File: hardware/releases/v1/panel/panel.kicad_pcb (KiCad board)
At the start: 4 copper layers, 124.5 x 55.6 mm, 171 parts, among them J1 12-32V + RS485, J101 Main board, J102 XD_North, J103 XD_East, J104 XD_South, J105 XD_West, J106 PIEZO_NE, J107 PIEZO_NW, J108 PIEZO_SW, J109 PIEZO_SE, J110 DOME_SOCKET, J111 AUX 5V_HEAT, J2 Crown board, J201 Probe T-Header SMD, J3 Probe board, J301 CROWN_RISER, J4 PMSA003I PM, J401 Main board, J402 Reflector T-Socket SMD, J5 Power board, J501 Main board, Q1 AO3400A, Q401 AO3400A, SW1 SERVICE, U101 SN74LVC2G04DBVR, U102 CD4052BM96, U103 TLV9062IDR, U104 LM393DR2G, U105 TLV9062IDR, U106 MMC5603NJ, U2 LM66100, U3 XIAO ESP32C6, U301 LTR-390UV-01, U302 TSL25911FN, U303 GUVB-C31SM, U4 ADS1115IDGSR, U401 SCD41-D-R2, U402 SGP41-D-R4, U403 SHT40-AD1F-R2, U404 LM393DR2G, U405 BMP585, U5 LSM6DS3TR-C, U501 SCT2430STER, U502 SCT2430STER, U6 AS3935-BQFT, U7 SP3485EN-L/TR, U8 SN74LVC2G04DBVR

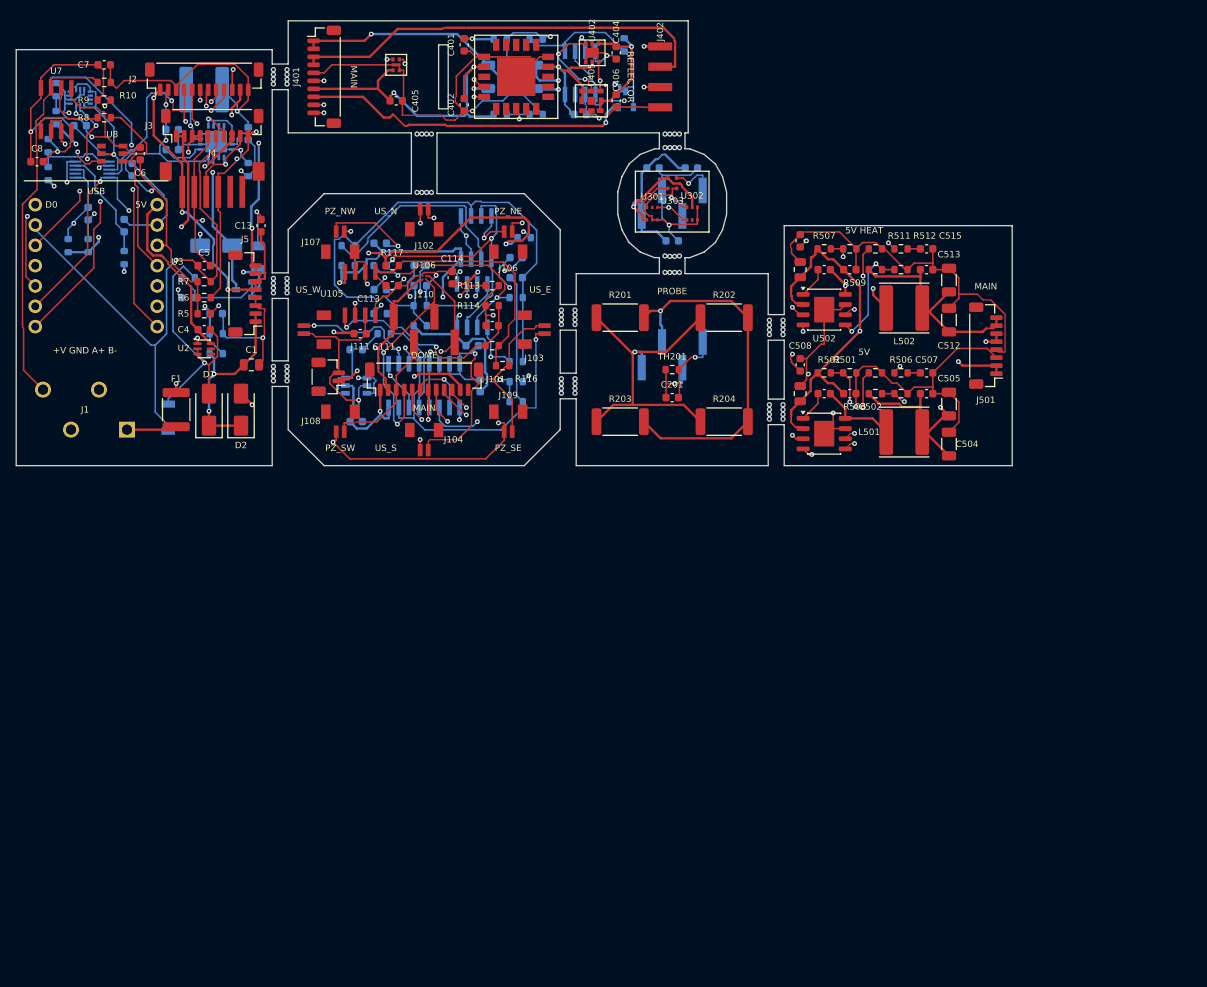
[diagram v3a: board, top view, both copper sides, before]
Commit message: Update documentation for 60V power system, STM32 crown board, 12V heaters, and expanded enclosure design
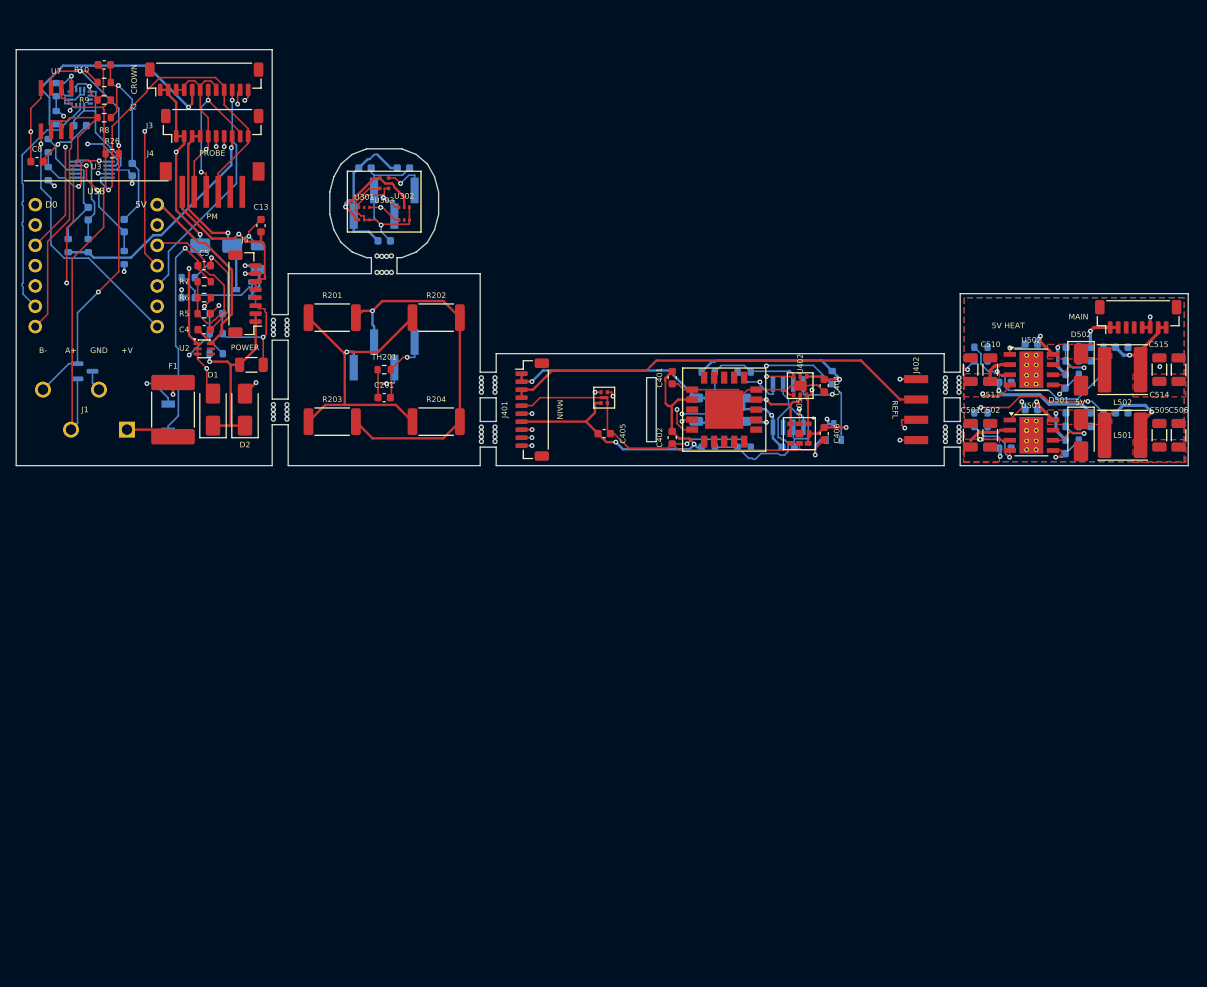
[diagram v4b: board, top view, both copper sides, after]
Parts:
- removed C10: 1u 50V, Capacitor_SMD:C_0603_1608Metric
- removed C101, C102, C103, C104, C105, C11, C110, C111, C114, C6: 100n 50V, Capacitor_SMD:C_0603_1608Metric
- removed C106, C107, C109: 47n 50V, Capacitor_SMD:C_0603_1608Metric
- removed C108, C112: 18p C0G 50V, Capacitor_SMD:C_0603_1608Metric
- removed C113: 220n 50V, Capacitor_SMD:C_0603_1608Metric
- removed C12: 470p C0G 50V, Capacitor_SMD:C_0603_1608Metric
- removed J101: Main board, Connector_JST:JST_SH_BM12B-SRSS-TB_1x12-1MP_P1.00mm_Vertical
- removed J102: XD_North, gateway_fp:JST_BM02B-SRSS-TB
- removed J103: XD_East, gateway_fp:JST_BM02B-SRSS-TB
- removed J104: XD_South, gateway_fp:JST_BM02B-SRSS-TB
- removed J105: XD_West, gateway_fp:JST_BM02B-SRSS-TB
- removed J106: PIEZO_NE, gateway_fp:JST_BM02B-SRSS-TB
- removed J107: PIEZO_NW, gateway_fp:JST_BM02B-SRSS-TB
- removed J108: PIEZO_SW, gateway_fp:JST_BM02B-SRSS-TB
- removed J109: PIEZO_SE, gateway_fp:JST_BM02B-SRSS-TB
- removed J110: DOME_SOCKET, gateway_fp:HX_PZ2.54-1x4P-SMD
- removed J111: AUX 5V_HEAT, Connector_JST:JST_SH_BM02B-SRSS-TB_1x02-1MP_P1.00mm_Vertical
- removed L2: 220uH, Inductor_SMD:L_Sunlord_SWPA6045S
- removed R101, R104, R105, R108, R113: 1k, Resistor_SMD:R_0603_1608Metric
- removed R102, R103, R107, R11, R111, R115: 10k, Resistor_SMD:R_0603_1608Metric
- removed R106, R109: 22k, Resistor_SMD:R_0603_1608Metric
- removed R110, R114, R117: 100k, Resistor_SMD:R_0603_1608Metric
- removed R112: 4k7, Resistor_SMD:R_0603_1608Metric
- removed R116: 20k, Resistor_SMD:R_0603_1608Metric
- removed U101, U8: SN74LVC2G04DBVR, gateway_fp:TI_SN74LVC2G04_SOT-23-6
- removed U102: CD4052BM96, gateway_fp:TI_CD4052BM96_SOIC-16
- removed U103, U105: TLV9062IDR, gateway_fp:TI_TLV9062IDR_SOIC-8
- removed U104: LM393DR2G, gateway_fp:ON_LM393DR2G_SOIC-8
- removed U106: MMC5603NJ, gateway_fp:MEMSIC_MMC5603NJ_WLCSP-4
- removed U6: AS3935-BQFT, gateway_fp:ScioSense_AS3935_QFN-16
- added C517: 18n 50V, Capacitor_SMD:C_0603_1608Metric, B.Cu at (135.1, -13.1)
- added C518: 68p C0G 50V, Capacitor_SMD:C_0603_1608Metric, B.Cu at (132.0, -14.8)
- added D4: PSM712, Package_TO_SOT_SMD:SOT-23, B.Cu at (8.60, -11.8)
- added D501: B360A, Diode_SMD:D_SMA, F.Cu at (133.1, -3.80)
- added D502: B360A, Diode_SMD:D_SMA, F.Cu at (133.1, -12.0)
- added R26: 120R, Resistor_SMD:R_0603_1608Metric, F.Cu at (12.0, -39.0)
- C1, C501: value 10u 50V -> 2u2 100V; footprint Capacitor_SMD:C_0805_2012Metric -> Capacitor_SMD:C_1206_3216Metric
- C502, C510, C511: value 100n 50V -> 2u2 100V; footprint Capacitor_SMD:C_0603_1608Metric -> Capacitor_SMD:C_1206_3216Metric
- C503: value 100n 50V -> 100n 100V; moved to B.Cu
- C504, C513: value 47u 10V -> 100n 50V; footprint Capacitor_SMD:C_1206_3216Metric -> Capacitor_SMD:C_0603_1608Metric; moved to B.Cu
- C506: value 100n 50V -> 47u 10V; footprint Capacitor_SMD:C_0603_1608Metric -> Capacitor_SMD:C_1206_3216Metric
- C507: value 3n3 50V -> 100n 50V; moved to B.Cu
- C508: value 22p C0G 50V -> 33n 50V; moved to B.Cu
- C509: value 10u 50V -> 68p C0G 50V; footprint Capacitor_SMD:C_0805_2012Metric -> Capacitor_SMD:C_0603_1608Metric; moved to B.Cu
- C512: value 47u 10V -> 100n 100V; footprint Capacitor_SMD:C_1206_3216Metric -> Capacitor_SMD:C_0603_1608Metric; moved to B.Cu
- C514: value 100n 50V -> 22u 25V; footprint Capacitor_SMD:C_0603_1608Metric -> Capacitor_SMD:C_1206_3216Metric
- C515: value 3n3 50V -> 22u 25V; footprint Capacitor_SMD:C_0603_1608Metric -> Capacitor_SMD:C_1206_3216Metric
- C516: value 22p C0G 50V -> 100n 50V; moved to B.Cu
- D1: value SMAJ33A -> SMAJ36A
- F1: footprint Fuse:Fuse_1812_4532Metric -> Fuse:Fuse_2920_7451Metric
- L502: value 8.2uH -> 22uH
- R10, R9: value 4k7 -> 390R
- R20: value 10k -> 30k
- R201, R202, R203, R204: value 27R -> 120R
- R401, R402: value 120R -> 680R
- R5, R6: value 4k7 -> 2k2
- R501, R507: value 51k -> 511k; moved to B.Cu
- R502, R508: value 10k -> 82k5; moved to B.Cu
- R503, R504: moved to B.Cu
- R505, R511: value 200k -> 130k; moved to B.Cu
- R506, R512: value 33k2 -> 6k49; moved to B.Cu
- R509: value 53k6 -> 140k; moved to B.Cu
- R510: value 10k2 -> 10k; moved to B.Cu
- R8: value 1k -> 10k
- U404: value LM393DR2G -> LM2903DR2G
- U501, U502: value SCT2430STER -> TPS54360DDAR; footprint Package_SO:SOIC-8-1EP_3.9x4.9mm_P1.27mm_EP2.514x3.2mm -> Package_SO:TI_SO-PowerPAD-8_ThermalVias
- moved J402 52.5 mm to (112.5, -7.00)
- moved C401 49.1 mm to (82.0, -11.0)
- moved C402 49.1 mm to (82.0, -3.50)
- moved C403 49.1 mm to (96.5, -2.30)
- moved C404 49.1 mm to (101.0, -10.0)
- moved C405 49.1 mm to (73.5, -4.00)
- moved C406 49.1 mm to (101.0, -4.00)
- moved J401 49.1 mm to (64.5, -7.00)
- moved Q401 49.1 mm to (102.2, -4.20)
- moved R401 49.1 mm to (85.0, -7.00)
- moved R402 49.1 mm to (91.0, -7.00)
- moved R403 49.1 mm to (86.5, -11.7)
- moved R404 49.1 mm to (86.5, -2.30)
- moved R405 49.1 mm to (91.0, -2.30)
- moved R406 49.1 mm to (102.0, -11.0)
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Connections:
- net REFLECTOR_+5V_HEAT renamed REFLECTOR_+12V_HEAT
- C403 pad 1: PROBE_+3V3 -> PROBE_+12V_HEAT
- C503 pad 1: POWER_LOGIC_BST -> POWER_VIN_PROT
- C503 pad 2: POWER_LOGIC_SW -> POWER_GND
- C504 pad 1: POWER_+5V -> POWER_LOGIC_BST
- C504 pad 2: POWER_GND -> POWER_LOGIC_SW
- C507 pad 1: POWER_LOGIC_CC -> POWER_+5V
- C508 pad 1: POWER_LOGIC_COMP -> POWER_LOGIC_CC
- C509 pad 1: POWER_VIN_PROT -> POWER_LOGIC_COMP
- C511 pad 1: POWER_HEAT_BST -> POWER_VIN_PROT
- C511 pad 2: POWER_HEAT_SW -> POWER_GND
- C512 pad 1: POWER_+5V_HEAT -> POWER_VIN_PROT
- C513 pad 1: POWER_+5V_HEAT -> POWER_HEAT_BST
- C513 pad 2: POWER_GND -> POWER_HEAT_SW
- C514 pad 1: POWER_+5V_HEAT -> POWER_+12V_HEAT
- C515 pad 1: POWER_HEAT_CC -> POWER_+12V_HEAT
- C516 pad 1: POWER_HEAT_COMP -> POWER_+12V_HEAT
- D3 pad 1: +5V_HEAT -> +12V_HEAT
- J2 pad 1: +5V -> +12V_HEAT
- J2 pad 10: RAIN_ADC -> CROWN_IRQ
- J2 pad 11: +5V_HEAT -> CROWN_NRST
- J2 pad 12: GND -> CROWN_BOOT0
- J2 pad 2: +3V3 -> +12V_HEAT
- J2 pad 4: I2C_SDA -> GND
- J2 pad 5: I2C_SCL -> +5V
- J2 pad 6: US_SEL_A -> GND
- J2 pad 7: US_SEL_B -> I2C_SDA
- J2 pad 8: US_TX -> GND
- J2 pad 9: US_RX -> I2C_SCL
- J3 pad 1: +5V_HEAT -> +12V_HEAT
- J3 pad 2: +5V_HEAT -> +12V_HEAT
- J401 pad 1: PROBE_+5V_HEAT -> PROBE_+12V_HEAT
- J401 pad 2: PROBE_+5V_HEAT -> PROBE_+12V_HEAT
- J402 pad 1: PROBE_+5V_HEAT -> PROBE_+12V_HEAT
- J5 pad 7: +5V_HEAT -> +12V_HEAT
- J5 pad 8: +5V_HEAT -> +12V_HEAT
- J501 pad 7: POWER_+5V_HEAT -> POWER_+12V_HEAT
- J501 pad 8: POWER_+5V_HEAT -> POWER_+12V_HEAT
- L502 pad 2: POWER_+5V_HEAT -> POWER_+12V_HEAT
- R20 pad 1: +5V_HEAT -> +12V_HEAT
- R401 pad 1: PROBE_+5V_HEAT -> PROBE_+12V_HEAT
- R402 pad 1: PROBE_+5V_HEAT -> PROBE_+12V_HEAT
- R509 pad 1: POWER_+5V_HEAT -> POWER_+12V_HEAT
- R8 pad 1: RS485_RO -> RS485_DE
- R8 pad 2: RS485_IO -> GND
- U3 pad 10: US_RX -> CROWN_IRQ
- U3 pad 11: RS485_IO -> CROWN_NRST
- U3 pad 3: RAIN_ADC -> CROWN_BOOT0
- U3 pad 7: US_SEL_A -> RS485_TX
- U3 pad 8: US_SEL_B -> RS485_RX
- U3 pad 9: US_TX -> RS485_DE
- U404 pad 8: PROBE_+3V3 -> PROBE_+12V_HEAT
- U7 pad 1: RS485_RO -> RS485_RX
- U7 pad 4: GND -> RS485_TX
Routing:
- net CROWN_GND: track 145.5 -> 0.00 mm, vias 6 -> 0
- net CROWN_PIEZO_IN: track 105.8 -> 0.00 mm, vias 5 -> 0
- net POWER_GND: track 102.1 -> 0.00 mm, vias 3 -> 1
- net CROWN_+5V: track 90.2 -> 0.00 mm, vias 5 -> 0
- net CROWN_US_VREF: track 72.9 -> 0.00 mm
- net +5V_HEAT: track 71.9 -> 0.00 mm, vias 6 -> 0
- net CROWN_+3V3: track 71.1 -> 0.00 mm, vias 4 -> 0
- net PROBE_+12V_HEAT: track 0.00 -> 63.3 mm, vias 0 -> 3
- net CROWN_US_RX: track 55.7 -> 0.00 mm, vias 3 -> 0
- net GND: track 183.2 -> 128.3 mm
- net PROBE_+5V_HEAT: track 53.7 -> 0.00 mm, vias 3 -> 0
- net +12V_HEAT: track 0.00 -> 53.0 mm, vias 0 -> 4
- net US_TX: track 44.0 -> 0.00 mm, vias 1 -> 0
- net US_RX: track 43.0 -> 0.00 mm, vias 1 -> 0
- net CROWN_XD_W: track 41.4 -> 0.00 mm, vias 3 -> 0
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- added copper zone on F.Cu, net POWER_+12V_HEAT
- added copper zone on F.Cu, net POWER_+5V
- added copper zone on B.Cu, net POWER_GND
- added copper zone on F.Cu, net POWER_GND
- added copper zone on F.Cu, net POWER_HEAT_SW
- added copper zone on F.Cu, net POWER_LOGIC_SW
- added copper zone on F.Cu, net POWER_VIN_PROT
- removed copper zone on In1.Cu, net CROWN_GND
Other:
- board size 124.5 x 55.6 mm -> 146.5 x 52 mm
- board text added: "+V"
- board text added: "A+"
- board text added: "B-"
- board text added: "GND"
- board text added: "POWER"
- board text added: "REFL"
- board text removed: "+V GND A+ B-"
- board text removed: "DOME"
- board text removed: "PZ_NE"
- board text removed: "PZ_NW"
- board text removed: "PZ_SE"
- board text removed: "PZ_SW"
- board text removed: "REFLECTOR"
- board text removed: "US_E"
- board text removed: "US_N"
- board text removed: "US_S"
- board text removed: "US_W"

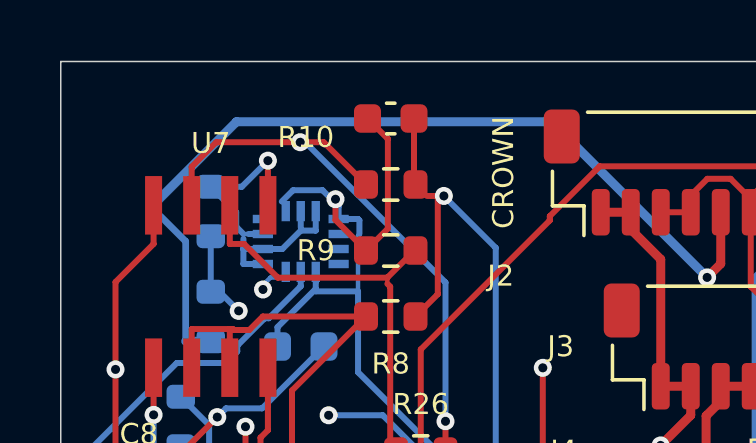
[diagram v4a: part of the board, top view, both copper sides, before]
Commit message: Update RS-485 to poll/response mode with multi-drop addressing, add crown protocol v2 with CRC-protected status, implement wind calibration and rain scaling, fix UCC27524 enable pull-down, add transducer adapter parts
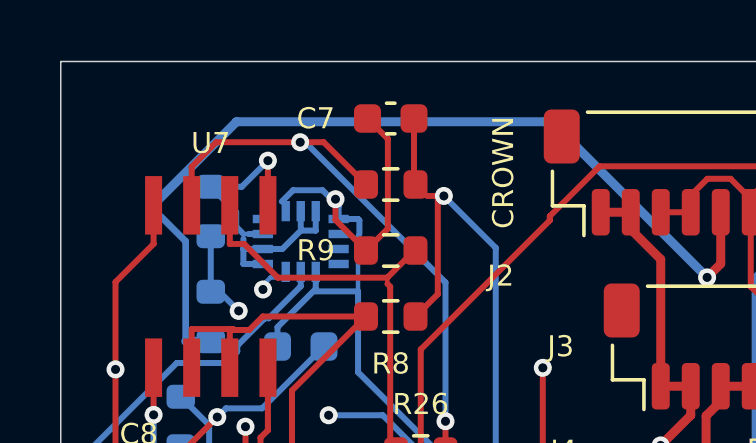
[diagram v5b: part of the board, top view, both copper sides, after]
